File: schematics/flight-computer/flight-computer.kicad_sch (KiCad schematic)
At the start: 80 parts, among them J101 BATT, J102 GPS, J103 TELEM, J104 Expansion Slot, J105 USB C, J106 SWD, J107 BLACKBOX, Q101 BSS138, U101 STM32F405RGT6, U102 MAX14787E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

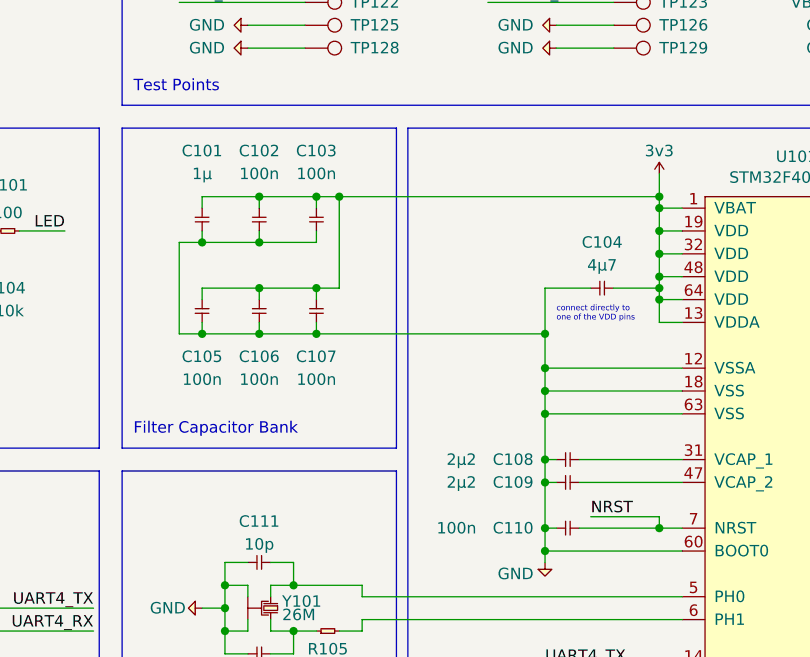
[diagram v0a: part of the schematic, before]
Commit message: Update passive order codes to 0402
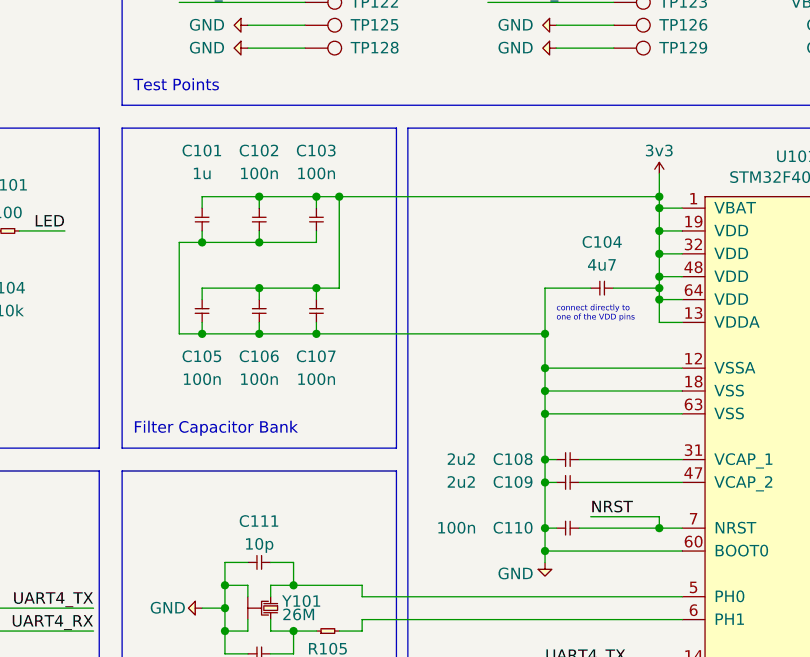
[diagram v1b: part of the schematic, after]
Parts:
- C101: value 1µ -> 1u; Farnell 1759436 -> 2218855
- C104: value 4µ7 -> 4u7; Farnell 2211173 -> 2346876
- C108, C109: value 2µ2 -> 2u2
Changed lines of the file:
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@@
       (effects (font (size 1.27 1.27)) (justify right))
     )
-    (property "Value" "2µ2" (id 1) (at 106.68 91.44 0)
+    (property "Value" "2u2" (id 1) (at 106.68 91.44 0)
       (effects (font (size 1.27 1.27)) (justify right))
     )
@@
       (effects (font (size 1.27 1.27)) (justify right))
     )
-    (property "Value" "2µ2" (id 1) (at 106.68 93.98 0)
+    (property "Value" "2u2" (id 1) (at 106.68 93.98 0)
       (effects (font (size 1.27 1.27)) (justify right))
     )
@@
     (in_bom yes) (on_board yes)
     (property "Reference" "C101" (id 0) (at 76.2 57.15 90))
-    (property "Value" "1µ" (id 1) (at 76.2 59.69 90))
+    (property "Value" "1u" (id 1) (at 76.2 59.69 90))
     (property "Footprint" "Strix:C_0402" (id 2) (at 76.2 66.04 0)
       (effects (font (size 1.27 1.27)) hide)
@@
       (effects (font (size 1.27 1.27)) hide)
     )
-    (property "Farnell" "1759436" (id 4) (at 76.2 66.04 0)
+    (property "Farnell" "2218855" (id 4) (at 76.2 66.04 0)
       (effects (font (size 1.27 1.27)) hide)
     )
@@
     (in_bom yes) (on_board yes)
     (property "Reference" "C104" (id 0) (at 120.65 67.31 0))
-    (property "Value" "4µ7" (id 1) (at 120.65 69.85 0))
+    (property "Value" "4u7" (id 1) (at 120.65 69.85 0))
     (property "Footprint" "Strix:C_0402" (id 2) (at 119.38 72.39 0)
       (effects (font (size 1.27 1.27)) hide)
@@
       (effects (font (size 1.27 1.27)) hide)
     )
-    (property "Farnell" "2211173" (id 4) (at 119.38 72.39 0)
+    (property "Farnell" "2346876" (id 4) (at 119.38 72.39 0)
       (effects (font (size 1.27 1.27)) hide)
     )
@@
     )
     (path "/00000000-0000-0000-0000-000060e7c4a9"
-      (reference "C101") (unit 1) (value "1µ") (footprint "Strix:C_0402")
+      (reference "C101") (unit 1) (value "1u") (footprint "Strix:C_0402")
     )
     (path "/00000000-0000-0000-0000-000060e7c4a2"
@@
     )
     (path "/00000000-0000-0000-0000-000060e7c4b0"
-      (reference "C104") (unit 1) (value "4µ7") (footprint "Strix:C_0402")
+      (reference "C104") (unit 1) (value "4u7") (footprint "Strix:C_0402")
     )
     (path "/00000000-0000-0000-0000-000060e7c494"
@@
     )
     (path "/00000000-0000-0000-0000-000060e7c46a"
-      (reference "C108") (unit 1) (value "2µ2") (footprint "Strix:C_0402")
+      (reference "C108") (unit 1) (value "2u2") (footprint "Strix:C_0402")
     )
     (path "/00000000-0000-0000-0000-000060e7c471"
-      (reference "C109") (unit 1) (value "2µ2") (footprint "Strix:C_0402")
+      (reference "C109") (unit 1) (value "2u2") (footprint "Strix:C_0402")
     )
     (path "/00000000-0000-0000-0000-0000613d0152"

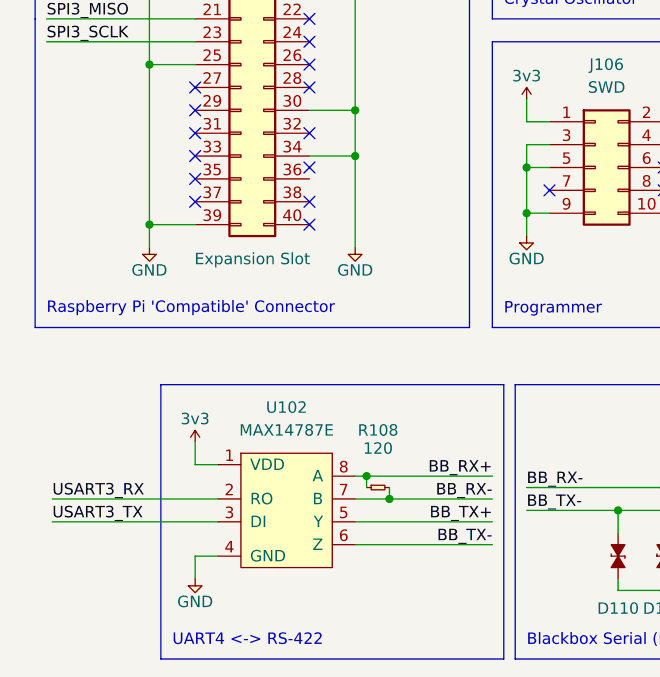
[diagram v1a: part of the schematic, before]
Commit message: Minor changes to pass ERC
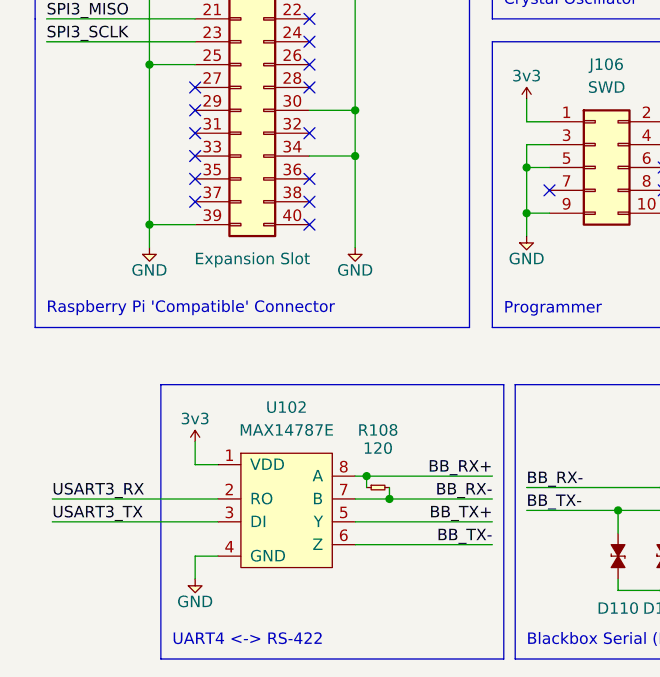
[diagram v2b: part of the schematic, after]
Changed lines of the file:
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@@
   (no_connect (at 46.99 148.59))
   (no_connect (at 46.99 146.05))
-  (no_connect (at 46.99 142.24))
+  (no_connect (at 46.99 143.51))
   (no_connect (at 46.99 138.43))
   (no_connect (at 46.99 118.11))
@@
     (stroke (width 0) (type default) (color 0 0 0 0))
   )
-  (wire (pts (xy 36.83 185.42) (xy 34.29 185.42))
-    (stroke (width 0) (type default) (color 0 0 0 0))
-  )
   (wire (pts (xy 76.2 72.39) (xy 82.55 72.39))
     (stroke (width 0) (type default) (color 0 0 0 0))
@@
     (stroke (width 0) (type default) (color 0 0 0 0))
   )
+  (wire (pts (xy 34.29 185.42) (xy 36.83 185.42))
+    (stroke (width 0) (type default) (color 0 0 0 0))
+  )
   (wire (pts (xy 81.28 189.23) (xy 86.36 189.23))
     (stroke (width 0) (type default) (color 0 0 0 0))
@@
     (pin "2")
   )
-  (symbol (lib_name "TestPoint_13") (lib_id "Strix:TestPoint") (at 156.21 30.48 270) (unit 1)
+  (symbol (lib_id "Strix:TestPoint") (at 156.21 30.48 270) (unit 1)
     (in_bom yes) (on_board yes)
     (property "Reference" "TP112" (id 0) (at 161.29 30.48 90)
@@
     (pin "1")
   )
-  (symbol (lib_name "TestPoint_12") (lib_id "Strix:TestPoint") (at 156.21 35.56 270) (unit 1)
+  (symbol (lib_id "Strix:TestPoint") (at 156.21 35.56 270) (unit 1)
     (in_bom yes) (on_board yes)
     (property "Reference" "TP118" (id 0) (at 161.29 35.56 90)
@@
     (pin "1")
   )
-  (symbol (lib_name "TestPoint_7") (lib_id "Strix:TestPoint") (at 87.63 22.86 270) (unit 1)
+  (symbol (lib_id "Strix:TestPoint") (at 87.63 22.86 270) (unit 1)
     (in_bom yes) (on_board yes)
     (property "Reference" "TP101" (id 0) (at 92.71 22.86 90)
@@
     (pin "1")
   )
-  (symbol (lib_name "TestPoint_20") (lib_id "Strix:TestPoint") (at 121.92 27.94 270) (unit 1)
+  (symbol (lib_id "Strix:TestPoint") (at 121.92 27.94 270) (unit 1)
     (in_bom yes) (on_board yes)
     (property "Reference" "TP108" (id 0) (at 127 27.94 90)
@@
     (pin "1")
   )
-  (symbol (lib_name "TestPoint_25") (lib_id "Strix:TestPoint") (at 87.63 40.64 270) (unit 1)
+  (symbol (lib_id "Strix:TestPoint") (at 87.63 40.64 270) (unit 1)
     (in_bom yes) (on_board yes)
     (property "Reference" "TP122" (id 0) (at 92.71 40.64 90)
@@
     (pin "1")
   )
-  (symbol (lib_name "TestPoint_24") (lib_id "Strix:TestPoint") (at 87.63 43.18 270) (unit 1)
+  (symbol (lib_id "Strix:TestPoint") (at 87.63 43.18 270) (unit 1)
     (in_bom yes) (on_board yes)
     (property "Reference" "TP125" (id 0) (at 92.71 43.18 90)
@@
     (pin "2")
   )
-  (symbol (lib_name "TestPoint_17") (lib_id "Strix:TestPoint") (at 156.21 22.86 270) (unit 1)
+  (symbol (lib_id "Strix:TestPoint") (at 156.21 22.86 270) (unit 1)
     (in_bom yes) (on_board yes)
     (property "Reference" "TP103" (id 0) (at 161.29 22.86 90)
@@
     (pin "1")
   )
-  (symbol (lib_name "TestPoint_8") (lib_id "Strix:TestPoint") (at 156.21 38.1 270) (unit 1)
+  (symbol (lib_id "Strix:TestPoint") (at 156.21 38.1 270) (unit 1)
     (in_bom yes) (on_board yes)
     (property "Reference" "TP121" (id 0) (at 161.29 38.1 90)
@@
     (pin "2")
   )
-  (symbol (lib_name "TestPoint_18") (lib_id "Strix:TestPoint") (at 121.92 35.56 270) (unit 1)
+  (symbol (lib_id "Strix:TestPoint") (at 121.92 35.56 270) (unit 1)
     (in_bom yes) (on_board yes)
     (property "Reference" "TP117" (id 0) (at 127 35.56 90)
@@
     (pin "1")
   )
-  (symbol (lib_name "TestPoint_1") (lib_id "Strix:TestPoint") (at 87.63 38.1 270) (unit 1)
+  (symbol (lib_id "Strix:TestPoint") (at 87.63 38.1 270) (unit 1)
     (in_bom yes) (on_board yes)
     (property "Reference" "TP119" (id 0) (at 92.71 38.1 90)
@@
     (pin "1")
   )
-  (symbol (lib_name "TestPoint_19") (lib_id "Strix:TestPoint") (at 121.92 30.48 270) (unit 1)
+  (symbol (lib_id "Strix:TestPoint") (at 121.92 30.48 270) (unit 1)
     (in_bom yes) (on_board yes)
     (property "Reference" "TP111" (id 0) (at 127 30.48 90)
@@
     (pin "2")
   )
-  (symbol (lib_name "TestPoint_2") (lib_id "Strix:TestPoint") (at 87.63 30.48 270) (unit 1)
+  (symbol (lib_id "Strix:TestPoint") (at 87.63 30.48 270) (unit 1)
     (in_bom yes) (on_board yes)
     (property "Reference" "TP110" (id 0) (at 92.71 30.48 90)
@@
     (pin "1")
   )
-  (symbol (lib_name "TestPoint_23") (lib_id "Strix:TestPoint") (at 87.63 45.72 270) (unit 1)
+  (symbol (lib_id "Strix:TestPoint") (at 87.63 45.72 270) (unit 1)
     (in_bom yes) (on_board yes)
     (property "Reference" "TP128" (id 0) (at 92.71 45.72 90)
@@
     (pin "1")
   )
-  (symbol (lib_name "TestPoint_26") (lib_id "Strix:TestPoint") (at 121.92 40.64 270) (unit 1)
+  (symbol (lib_id "Strix:TestPoint") (at 121.92 40.64 270) (unit 1)
     (in_bom yes) (on_board yes)
     (property "Reference" "TP123" (id 0) (at 127 40.64 90)
@@
     (pin "1")
   )
-  (symbol (lib_name "TestPoint_29") (lib_id "Strix:TestPoint") (at 121.92 22.86 270) (unit 1)
+  (symbol (lib_id "Strix:TestPoint") (at 121.92 22.86 270) (unit 1)
     (in_bom yes) (on_board yes)
     (property "Reference" "TP102" (id 0) (at 127 22.86 90)
@@
     (pin "2")
   )
-  (symbol (lib_name "TestPoint_28") (lib_id "Strix:TestPoint") (at 121.92 43.18 270) (unit 1)
+  (symbol (lib_id "Strix:TestPoint") (at 121.92 43.18 270) (unit 1)
     (in_bom yes) (on_board yes)
     (property "Reference" "TP126" (id 0) (at 127 43.18 90)
@@
     (pin "1")
   )
-  (symbol (lib_name "TestPoint_27") (lib_id "Strix:TestPoint") (at 121.92 45.72 270) (unit 1)
+  (symbol (lib_id "Strix:TestPoint") (at 121.92 45.72 270) (unit 1)
     (in_bom yes) (on_board yes)
     (property "Reference" "TP129" (id 0) (at 127 45.72 90)
@@
     (pin "1")
   )
-  (symbol (lib_name "TestPoint_11") (lib_id "Strix:TestPoint") (at 156.21 45.72 270) (unit 1)
+  (symbol (lib_id "Strix:TestPoint") (at 156.21 45.72 270) (unit 1)
     (in_bom yes) (on_board yes)
     (property "Reference" "TP130" (id 0) (at 161.29 45.72 90)
@@
     (pin "1")
   )
-  (symbol (lib_name "TestPoint_15") (lib_id "Strix:TestPoint") (at 156.21 33.02 270) (unit 1)
+  (symbol (lib_id "Strix:TestPoint") (at 156.21 33.02 270) (unit 1)
     (in_bom yes) (on_board yes)
     (property "Reference" "TP115" (id 0) (at 161.29 33.02 90)
@@
     (pin "9")
   )
-  (symbol (lib_name "TestPoint_22") (lib_id "Strix:TestPoint") (at 121.92 33.02 270) (unit 1)
+  (symbol (lib_id "Strix:TestPoint") (at 121.92 33.02 270) (unit 1)
     (in_bom yes) (on_board yes)
     (property "Reference" "TP114" (id 0) (at 127 33.02 90)
@@
     (pin "1")
   )
-  (symbol (lib_name "TestPoint_16") (lib_id "Strix:TestPoint") (at 156.21 27.94 270) (unit 1)
+  (symbol (lib_id "Strix:TestPoint") (at 156.21 27.94 270) (unit 1)
     (in_bom yes) (on_board yes)
     (property "Reference" "TP109" (id 0) (at 161.29 27.94 90)
@@
     (pin "1")
   )
-  (symbol (lib_name "TestPoint_6") (lib_id "Strix:TestPoint") (at 87.63 27.94 270) (unit 1)
+  (symbol (lib_id "Strix:TestPoint") (at 87.63 27.94 270) (unit 1)
     (in_bom yes) (on_board yes)
     (property "Reference" "TP107" (id 0) (at 92.71 27.94 90)
@@
     (pin "1")
   )
-  (symbol (lib_name "TestPoint_4") (lib_id "Strix:TestPoint") (at 87.63 35.56 270) (unit 1)
+  (symbol (lib_id "Strix:TestPoint") (at 87.63 35.56 270) (unit 1)
     (in_bom yes) (on_board yes)
     (property "Reference" "TP116" (id 0) (at 92.71 35.56 90)
@@
     (pin "1")
   )
-  (symbol (lib_name "TestPoint_10") (lib_id "Strix:TestPoint") (at 156.21 43.18 270) (unit 1)
+  (symbol (lib_id "Strix:TestPoint") (at 156.21 43.18 270) (unit 1)
     (in_bom yes) (on_board yes)
     (property "Reference" "TP127" (id 0) (at 161.29 43.18 90)
@@
     (pin "2")
   )
-  (symbol (lib_name "TestPoint_5") (lib_id "Strix:TestPoint") (at 87.63 25.4 270) (unit 1)
+  (symbol (lib_id "Strix:TestPoint") (at 87.63 25.4 270) (unit 1)
     (in_bom yes) (on_board yes)
     (property "Reference" "TP104" (id 0) (at 92.71 25.4 90)
@@
     (pin "1")
   )
-  (symbol (lib_name "TestPoint_9") (lib_id "Strix:TestPoint") (at 156.21 40.64 270) (unit 1)
+  (symbol (lib_id "Strix:TestPoint") (at 156.21 40.64 270) (unit 1)
     (in_bom yes) (on_board yes)
     (property "Reference" "TP124" (id 0) (at 161.29 40.64 90)
@@
     (pin "1")
   )
-  (symbol (lib_name "TestPoint_3") (lib_id "Strix:TestPoint") (at 87.63 33.02 270) (unit 1)
+  (symbol (lib_id "Strix:TestPoint") (at 87.63 33.02 270) (unit 1)
     (in_bom yes) (on_board yes)
     (property "Reference" "TP113" (id 0) (at 92.71 33.02 90)
@@
     (pin "1")
   )
-  (symbol (lib_name "TestPoint_21") (lib_id "Strix:TestPoint") (at 121.92 25.4 270) (unit 1)
+  (symbol (lib_id "Strix:TestPoint") (at 121.92 25.4 270) (unit 1)
     (in_bom yes) (on_board yes)
     (property "Reference" "TP105" (id 0) (at 127 25.4 90)
@@
     (pin "1")
   )
-  (symbol (lib_name "TestPoint_14") (lib_id "Strix:TestPoint") (at 156.21 25.4 270) (unit 1)
+  (symbol (lib_id "Strix:TestPoint") (at 156.21 25.4 270) (unit 1)
     (in_bom yes) (on_board yes)
     (property "Reference" "TP106" (id 0) (at 161.29 25.4 90)
@@
   )
   (symbol_instances
+    (path "/0560d9e6-7a86-479d-84fc-0ec915d62cea/7cd622a3-c43b-4101-80f5-22ce2878554d"
+      (reference "#FLG0104") (unit 1) (value "PWR") (footprint "")
+    )
+    (path "/00000000-0000-0000-0000-0000619fd90a/c6c1c5c4-28ef-43f4-a670-14df890fb64e"
+      (reference "#FLG0105") (unit 1) (value "PWR") (footprint "")
+    )
     (path "/00000000-0000-0000-0000-000060d03c1d"
       (reference "#PWR0101") (unit 1) (value "GND") (footprint "")
@@
       (reference "U301") (unit 1) (value "Si4463") (footprint "Strix:Si4463")
     )
-    (path "/00000000-0000-0000-0000-0000611291b2/00000000-0000-0000-0000-0000613a31e6"
+    (path "/00000000-0000-0000-0000-0000611291b2/f8a26d2e-ad7f-4b08-8ad1-68361c6a3ac6"
       (reference "U302") (unit 1) (value "MAX-M8") (footprint "Strix:MAX-M8")
     )

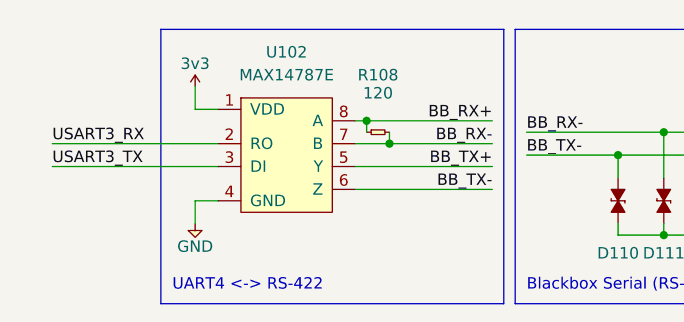
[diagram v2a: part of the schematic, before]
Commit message: Fix typo in schematic
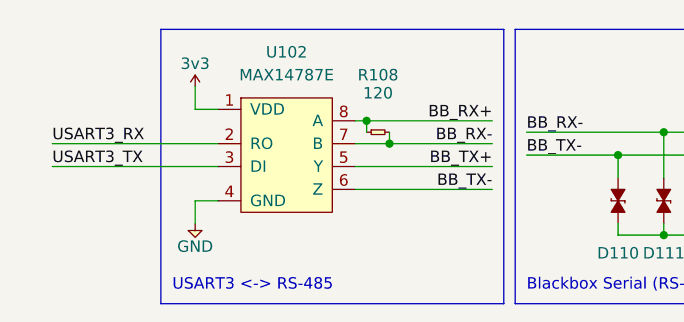
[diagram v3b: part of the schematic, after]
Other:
- note added: "USART3 <-> RS-485"
- note removed: "UART4 <-> RS-422"
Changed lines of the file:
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@@
     (effects (font (size 1.27 1.27)) (justify left bottom))
   )
-  (text "UART4 <-> RS-422" (at 31.75 195.58 0)
+  (text "USART3 <-> RS-485" (at 31.75 195.58 0)
     (effects (font (size 1.27 1.27)) (justify left bottom))
   )
